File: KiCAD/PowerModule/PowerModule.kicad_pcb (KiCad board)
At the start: 2 copper layers, 90 x 70 mm, 41 parts, among them J1 GPU, J2 BATTERY, J3 BUS, J4 MONITOR, J5 MASTER, J6 Conn_01x02, J7 Conn_01x02, Q3 AO3401A, Q5 AO3401A, U2 INA219BxDCN, U3 INA219BxDCN, U4 INA219BxDCN

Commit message: 塗りつぶしとクリアランスの設定を変更．エラーは無し．
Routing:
- net +3.3V: track 67.1 -> 70.2 mm, vias 1 -> 3
- net GND: vias 59 -> 58
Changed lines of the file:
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@@
 	)
 	(setup
+		(stackup
+			(layer "F.SilkS"
+				(type "Top Silk Screen")
+			)
+			(layer "F.Paste"
+				(type "Top Solder Paste")
+			)
+			(layer "F.Mask"
+				(type "Top Solder Mask")
+				(thickness 0.01)
+			)
+			(layer "F.Cu"
+				(type "copper")
+				(thickness 0.035)
+			)
+			(layer "dielectric 1"
+				(type "core")
+				(thickness 1.51)
+				(material "FR4")
+				(epsilon_r 4.5)
+				(loss_tangent 0.02)
+			)
+			(layer "B.Cu"
+				(type "copper")
+				(thickness 0.035)
+			)
+			(layer "B.Mask"
+				(type "Bottom Solder Mask")
+				(thickness 0.01)
+			)
+			(layer "B.Paste"
+				(type "Bottom Solder Paste")
+			)
+			(layer "B.SilkS"
+				(type "Bottom Silk Screen")
+			)
+			(copper_finish "None")
+			(dielectric_constraints no)
+		)
 		(pad_to_mask_clearance 0)
 		(allow_soldermask_bridges_in_footprints no)
@@
 	)
 	(via
-		(at 176.19764 134.36)
-		(size 0.6)
-		(drill 0.3)
-		(layers "F.Cu" "B.Cu")
-		(free yes)
-		(net 2)
-	)
-	(via
 		(at 144 134)
 		(size 0.6)
@@
 	)
 	(segment
-		(start 122.4 96.05)
-		(end 123.35 96.05)
-		(width 0.25)
+		(start 124.675 93.257)
+		(end 124.675 94.1)
+		(width 0.2)
 		(layer "F.Cu")
 		(net 8)
 	)
 	(segment
-		(start 124.675 94.174)
-		(end 124.675 94.1)
-		(width 0.25)
+		(start 122.428 96.078)
+		(end 122.4 96.05)
+		(width 0.2)
 		(layer "F.Cu")
 		(net 8)
@@
 	)
 	(segment
+		(start 122.428 96.774)
+		(end 122.428 96.078)
+		(width 0.2)
+		(layer "F.Cu")
+		(net 8)
+	)
+	(segment
 		(start 124.037501 99.55)
 		(end 124.7 99.55)
@@
 	)
 	(segment
-		(start 123.35 96.05)
-		(end 123.5 95.9)
-		(width 0.25)
-		(layer "F.Cu")
-		(net 8)
-	)
-	(segment
 		(start 130.8375 94.1)
 		(end 130.8375 99.6)
@@
 	)
 	(segment
-		(start 123.5 95.9)
-		(end 123.5 94.5)
-		(width 0.25)
-		(layer "F.Cu")
-		(net 8)
-	)
-	(segment
 		(start 130.8375 99.6)
 		(end 130.8375 106.2)
@@
 	)
 	(segment
+		(start 124.714 93.218)
+		(end 124.675 93.257)
+		(width 0.2)
+		(layer "F.Cu")
+		(net 8)
+	)
+	(segment
 		(start 146.9875 124.4875)
 		(end 146.9875 122.4)
@@
 	)
 	(segment
-		(start 123.5 94.5)
-		(end 123.826 94.174)
-		(width 0.25)
-		(layer "F.Cu")
-		(net 8)
-	)
-	(segment
 		(start 130.8375 99.6)
 		(end 130.0375 98.8)
@@
 		(net 8)
 	)
-	(segment
-		(start 123.826 94.174)
-		(end 124.675 94.174)
-		(width 0.25)
-		(layer "F.Cu")
+	(via
+		(at 130.9 110.9)
+		(size 0.6)
+		(drill 0.3)
+		(layers "F.Cu" "B.Cu")
 		(net 8)
 	)
 	(via
-		(at 130.9 110.9)
+		(at 122.428 96.774)
 		(size 0.6)
 		(drill 0.3)
@@
 		(net 8)
 	)
+	(via
+		(at 124.714 93.218)
+		(size 0.6)
+		(drill 0.3)
+		(layers "F.Cu" "B.Cu")
+		(net 8)
+	)
+	(segment
+		(start 122.428 96.774)
+		(end 123.19 96.774)
+		(width 0.2)
+		(layer "B.Cu")
+		(net 8)
+	)
 	(segment
 		(start 132.7 111.6)
@@
 	)
 	(segment
+		(start 123.952 93.218)
+		(end 124.714 93.218)
+		(width 0.2)
+		(layer "B.Cu")
+		(net 8)
+	)
+	(segment
 		(start 131.6 111.6)
 		(end 132.7 111.6)
@@
 	)
 	(segment
+		(start 123.444 93.726)
+		(end 123.952 93.218)
+		(width 0.2)
+		(layer "B.Cu")
+		(net 8)
+	)
+	(segment
+		(start 123.19 96.774)
+		(end 123.444 96.52)
+		(width 0.2)
+		(layer "B.Cu")
+		(net 8)
+	)
+	(segment
 		(start 130.9 110.9)
 		(end 131.6 111.6)
@@
 	)
 	(segment
+		(start 123.444 96.52)
+		(end 123.444 93.726)
+		(width 0.2)
+		(layer "B.Cu")
+		(net 8)
+	)
+	(segment
 		(start 145.65 124.55)
 		(end 147 124.55)
@@
 		(layers "F.Cu" "B.Cu")
 		(hatch edge 0.5)
-		(connect_pads
+		(connect_pads yes
 			(clearance 0.25)
 		)

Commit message: Power Build-1,Battery Build-1完成
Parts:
- added G***: LOGO, LOGO, B.Cu at (162.9, 131.2)
- added G***: LOGO, LOGO, B.Cu at (136.9, 131.8)
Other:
- outline, holes or cut-outs redrawn
- board text added: "CAPACITOR"
- board text added: "Power Module Build-1"
- board text added: "SUBARU"
- board text added: "Tokai Student Rocket Project"
- board text added: "U1"
- board text added: "V1.3"
- board text removed: "capacitor"

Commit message: 取り付け穴位置を更新
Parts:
- J7: value Conn_01x02 -> DF1B-2S-2.5R
- moved H1 5.83 mm to (120.0, 128.0)
- moved H2 5.83 mm to (120.0, 72.0)
- moved H3 5.83 mm to (180.0, 128.0)
- moved H4 5.83 mm to (180.0, 72.0)
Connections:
- H1 pad 1: GND -> (no net)
- H2 pad 1: GND -> (no net)
- H3 pad 1: GND -> (no net)
- H4 pad 1: GND -> (no net)
- J7 pad 1: Net-(D3-A) -> GND
- J7 pad 2: unconnected-(J7-Pin_2-Pad2) -> Net-(D3-A)
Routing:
- net VREF_T1: track 26.9 -> 15.8 mm
- net Net-(D3-A): track 19.5 -> 22.4 mm
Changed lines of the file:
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@@
 	(net 33 "Net-(U1-PGD)")
 	(net 34 "+5V")
-	(net 35 "unconnected-(J7-Pin_2-Pad2)")
 	(footprint "Resistor_SMD:R_0603_1608Metric"
 		(layer "F.Cu")
@@
 	(footprint "MountingHole:MountingHole_3.2mm_M3_DIN965_Pad_TopBottom"
 		(layer "F.Cu")
-		(at 125 125)
+		(at 120 128)
 		(descr "Mounting Hole 3.2mm, M3, DIN965")
 		(tags "mounting hole 3.2mm m3 din965")
@@
 			(layers "*.Cu" "*.Mask")
 			(remove_unused_layers no)
-			(net 2 "GND")
 		)
 		(pad "1" connect circle
@@
 			(size 5.6 5.6)
 			(layers "F.Cu" "F.Mask")
-			(net 2 "GND")
 		)
 		(pad "1" connect circle
@@
 			(size 5.6 5.6)
 			(layers "B.Cu" "B.Mask")
-			(net 2 "GND")
 		)
 		(embedded_fonts no)
@@
 	(footprint "MountingHole:MountingHole_3.2mm_M3_DIN965_Pad_TopBottom"
 		(layer "F.Cu")
-		(at 175 75)
+		(at 180 72)
 		(descr "Mounting Hole 3.2mm, M3, DIN965")
 		(tags "mounting hole 3.2mm m3 din965")
@@
 			(layers "*.Cu" "*.Mask")
 			(remove_unused_layers no)
-			(net 2 "GND")
 		)
 		(pad "1" connect circle
@@
 			(size 5.6 5.6)
 			(layers "F.Cu" "F.Mask")
-			(net 2 "GND")
 		)
 		(pad "1" connect circle
@@
 			(size 5.6 5.6)
 			(layers "B.Cu" "B.Mask")
-			(net 2 "GND")
 		)
 		(embedded_fonts no)
@@
 	(footprint "MountingHole:MountingHole_3.2mm_M3_DIN965_Pad_TopBottom"
 		(layer "F.Cu")
-		(at 175 125)
+		(at 180 128)
 		(descr "Mounting Hole 3.2mm, M3, DIN965")
 		(tags "mounting hole 3.2mm m3 din965")
@@
 			(layers "*.Cu" "*.Mask")
 			(remove_unused_layers no)
-			(net 2 "GND")
 		)
 		(pad "1" connect circle
@@
 			(size 5.6 5.6)
 			(layers "F.Cu" "F.Mask")
-			(net 2 "GND")
 		)
 		(pad "1" connect circle
@@
 			(size 5.6 5.6)
 			(layers "B.Cu" "B.Mask")
-			(net 2 "GND")
 		)
 		(embedded_fonts no)
@@
 			)
 		)
-		(property "Value" "Conn_01x02"
+		(property "Value" "DF1B-2S-2.5R"
 			(at 0 -8.1 180)
 			(unlocked yes)
@@
 			(layers "*.Cu" "*.Mask")
 			(remove_unused_layers no)
-			(net 9 "Net-(D3-A)")
+			(net 2 "GND")
 			(pinfunction "Pin_1")
 			(pintype "passive")
@@
 			(layers "*.Cu" "*.Mask")
 			(remove_unused_layers no)
-			(net 35 "unconnected-(J7-Pin_2-Pad2)")
+			(net 9 "Net-(D3-A)")
 			(pinfunction "Pin_2")
-			(pintype "passive+no_connect")
+			(pintype "passive")
 			(solder_mask_margin 0.1016)
 			(thermal_bridge_angle 45)
@@
 	(footprint "MountingHole:MountingHole_3.2mm_M3_DIN965_Pad_TopBottom"
 		(layer "F.Cu")
-		(at 125 75)
+		(at 120 72)
 		(descr "Mounting Hole 3.2mm, M3, DIN965")
 		(tags "mounting hole 3.2mm m3 din965")
@@
 			(layers "*.Cu" "*.Mask")
 			(remove_unused_layers no)
-			(net 2 "GND")
 		)
 		(pad "1" connect circle
@@
 			(size 5.6 5.6)
 			(layers "F.Cu" "F.Mask")
-			(net 2 "GND")
 		)
 		(pad "1" connect circle
@@
 			(size 5.6 5.6)
 			(layers "B.Cu" "B.Mask")
-			(net 2 "GND")
 		)
 		(embedded_fonts no)
@@
 	)
 	(gr_text "BAT SW"
-		(at 151.8 66.6 180)
+		(at 151.962 54.483 180)
 		(layer "F.SilkS" knockout)
 		(effects
@@
 	)
 	(gr_text "BATTERY\n"
-		(at 133.9 66.6 180)
+		(at 127.254 55.118 180)
 		(layer "F.SilkS" knockout)
 		(effects
@@
 	)
 	(gr_text "SW"
-		(at 160.038 66.5 180)
+		(at 161.036 54.61 180)
 		(layer "F.SilkS" knockout)
 		(effects
@@
 	)
 	(gr_text "CAPACITOR\n"
-		(at 142.9 66.8 180)
+		(at 142.962 58.674 180)
 		(layer "F.SilkS" knockout)
 		(effects
@@
 	)
 	(segment
-		(start 144.232 75.712)
-		(end 144.232 79.032)
+		(start 152.0875 84.2125)
+		(end 153.3 83)
 		(width 0.5)
 		(layer "F.Cu")
@@
 	)
 	(segment
-		(start 153.3 83)
-		(end 148.2 83)
+		(start 141.732 79.629)
+		(end 141.732 75.752)
 		(width 0.5)
 		(layer "F.Cu")
@@
 	)
 	(segment
-		(start 152.0875 84.2125)
-		(end 153.3 83)
+		(start 145.103 83)
+		(end 141.732 79.629)
 		(width 0.5)
 		(layer "F.Cu")
@@
 	)
 	(segment
-		(start 148.2 83)
-		(end 144.232 79.032)
+		(start 153.3 83)
+		(end 145.103 83)
+		(width 0.5)
+		(layer "F.Cu")
+		(net 9)
+	)
+	(segment
+		(start 141.732 75.752)
+		(end 141.692 75.712)
 		(width 0.5)
 		(layer "F.Cu")
@@
 	)
 	(segment
-		(start 154.6 129.2)
-		(end 154.6 123.2)
-		(width 0.2)
-		(layer "B.Cu")
-		(net 22)
-	)
-	(segment
-		(start 154.6 123.2)
-		(end 154.1 122.7)
+		(start 149.987 125.563)
+		(end 151 124.55)
 		(width 0.2)
 		(layer "B.Cu")
@@
 	)
 	(segment
-		(start 154.1 122.7)
-		(end 152.85 122.7)
+		(start 145.410668 132)
+		(end 149.987 127.423668)
 		(width 0.2)
 		(layer "B.Cu")
@@
 	)
 	(segment
-		(start 151.8 132)
-		(end 154.6 129.2)
+		(start 143.5 132)
+		(end 145.410668 132)
 		(width 0.2)
 		(layer "B.Cu")
@@
 	)
 	(segment
-		(start 152.85 122.7)
-		(end 151 124.55)
+		(start 149.987 127.423668)
+		(end 149.987 125.563)
 		(width 0.2)
 		(layer "B.Cu")
@@
 	)
 	(segment
-		(start 143.5 132)
-		(end 151.8 132)
-		(width 0.2)
-		(layer "B.Cu")
-		(net 22)
-	)
-	(segment
 		(start 158.73 77.73)
 		(end 158.73 75.712)
@@
 	)
 	(segment
-		(start 148.7839 126.149)
-		(end 149 126.149)
-		(width 0.2)
-		(layer "F.Cu")
-		(net 28)
-	)
-	(segment
 		(start 119.975 106.125)
 		(end 119.2 106.9)
@@
 		(layers "F.Cu" "B.Cu")
 		(hatch edge 0.5)
-		(connect_pads yes
+		(connect_pads
 			(clearance 0.25)
 		)
@@
 		(polygon
 			(pts
-				(xy 86.1 68) (xy 89.005402 145.4557) (xy 191.4 140.3) (xy 207 60.6) (xy 101.1 59.6)
+				(xy 122 60) (xy 100 80) (xy 100 120) (xy 120 140) (xy 180 140) (xy 200 120) (xy 200 80) (xy 180 60)
 			)
 		)

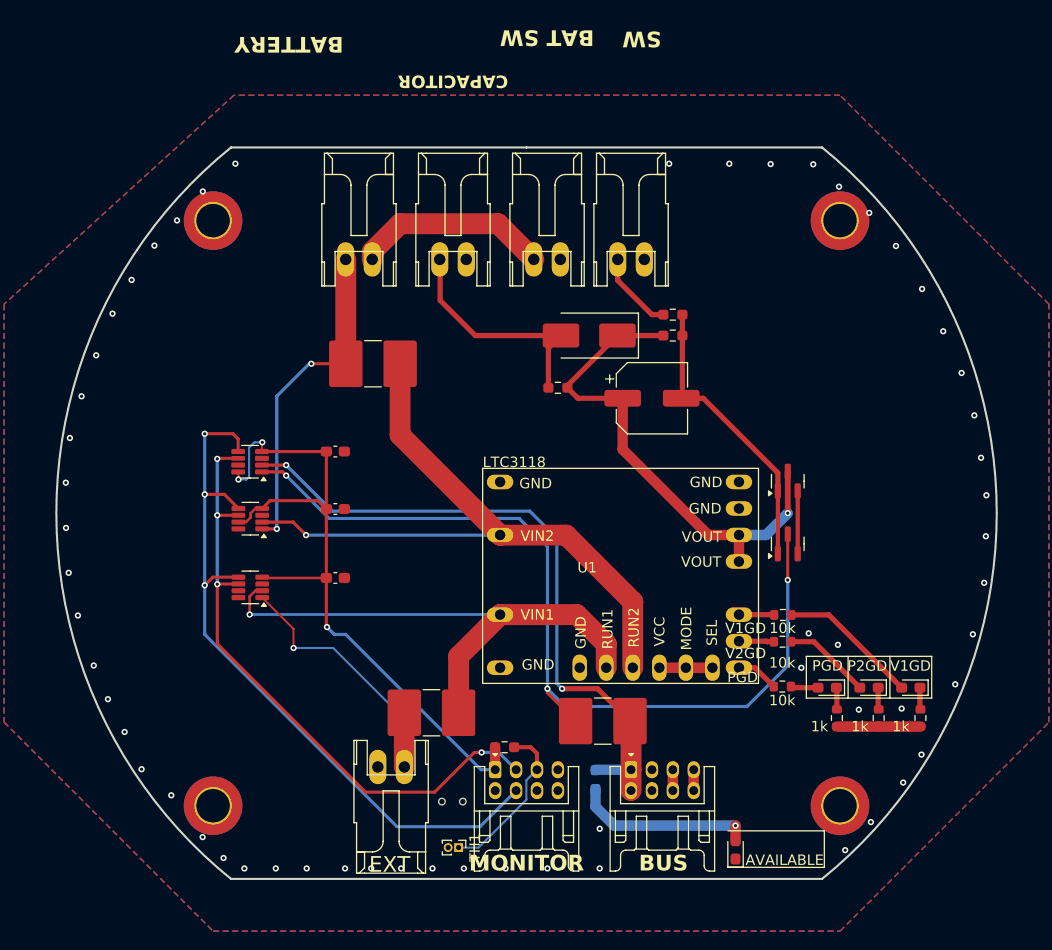
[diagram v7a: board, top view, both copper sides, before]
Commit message: 3Dモデルを組み合わせて結合試験する
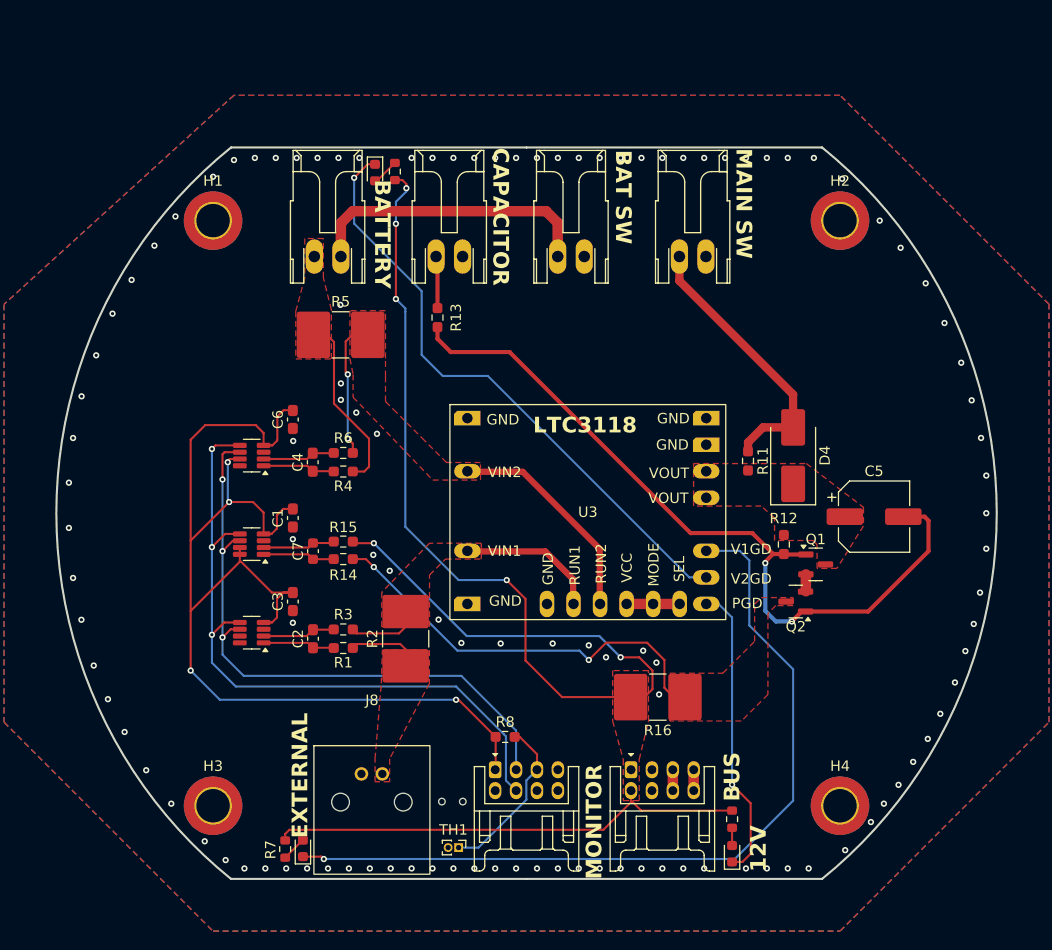
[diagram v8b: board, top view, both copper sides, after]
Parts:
- removed C16: 33uF, Capacitor_SMD:CP_Elec_6.3x5.9
- removed D5, D6: Orange, LED_SMD:LED_0603_1608Metric_Pad1.05x0.95mm_HandSolder
- removed D7: Green, LED_SMD:LED_0603_1608Metric_Pad1.05x0.95mm_HandSolder
- removed J1: GPU, TSRP_Connector_Hirose:DF1B-2S-2.5R
- removed Q3, Q5: AO3401A, Package_TO_SOT_SMD:SOT-23
- removed R17: 5.6kR, Resistor_SMD:R_0603_1608Metric_Pad0.98x0.95mm_HandSolder
- removed R18: 3.3kR, Resistor_SMD:R_0603_1608Metric_Pad0.98x0.95mm_HandSolder
- removed R19: 0.1R, Resistor_SMD:R_2816_7142Metric_Pad3.20x4.45mm_HandSolder
- added C1: 0.1uF, Capacitor_SMD:C_0603_1608Metric_Pad1.08x0.95mm_HandSolder, F.Cu at (127.6, 100.5)
- added C2: 0.1uF, Capacitor_SMD:C_0603_1608Metric_Pad1.08x0.95mm_HandSolder, F.Cu at (129.6, 112.0)
- added C3: 0.1uF, Capacitor_SMD:C_0603_1608Metric_Pad1.08x0.95mm_HandSolder, F.Cu at (127.6, 108.5)
- added C7: 0.1uF, Capacitor_SMD:C_0603_1608Metric, F.Cu at (129.6, 103.6)
- added D1: Orange, LED_SMD:LED_0603_1608Metric, F.Cu at (128.6, 132.1)
- added D2: Orange, LED_SMD:LED_0603_1608Metric, F.Cu at (135.5, 67.4)
- added J8: DF51-2P-2DS, TSRP_Connector_Hirose:DF51-2P-2DS, F.Cu at (135.2, 134.4)
- added Q1: AO3401A, Package_TO_SOT_SMD:SOT-23, F.Cu at (177.7, 104.9)
- added Q2: AO3401A, Package_TO_SOT_SMD:SOT-23, F.Cu at (175.8, 108.5)
- added R12: 5.6kR, Resistor_SMD:R_0603_1608Metric_Pad0.98x0.95mm_HandSolder, F.Cu at (174.6, 103.0)
- added R14: 10R, Resistor_SMD:R_0603_1608Metric_Pad0.98x0.95mm_HandSolder, F.Cu at (132.5, 104.4)
- added R15: 10R, Resistor_SMD:R_0603_1608Metric_Pad0.98x0.95mm_HandSolder, F.Cu at (132.5, 102.7)
- added R16: 0.1R, Resistor_SMD:R_2816_7142Metric_Pad3.20x4.45mm_HandSolder, F.Cu at (162.6, 117.6)
- added R4: 10R, Resistor_SMD:R_0603_1608Metric_Pad0.98x0.95mm_HandSolder, F.Cu at (132.5, 96.0)
- C5: value 0.1uF -> 33uF; footprint Capacitor_SMD:C_0603_1608Metric_Pad1.08x0.95mm_HandSolder -> Capacitor_SMD:CP_Elec_6.3x5.9
- D3: value SR54F -> Orange; footprint Diode_SMD:D_SMB_Handsoldering -> LED_SMD:LED_0603_1608Metric
- D4: value Orange -> SR54F; footprint LED_SMD:LED_0603_1608Metric_Pad1.05x0.95mm_HandSolder -> Diode_SMD:D_SMB_Handsoldering
- H1, H2, H3, H4: value MountingHole -> MountingHole_Pad
- J2: renamed from J6; value Conn_01x02 -> DF1B-2S-2.5R
- J3: renamed from J2; value BATTERY -> DF1B-2S-2.5R
- J5: renamed from J3; value BUS -> DF11-8DP-2DS
- J6: renamed from J5; value MASTER -> DF1B-2S-2.5R
- J7: renamed from J4; value MONITOR -> DF11-8DP-2DS
- R1: value 10k -> 10R; footprint Resistor_SMD:R_0603_1608Metric -> Resistor_SMD:R_0603_1608Metric_Pad0.98x0.95mm_HandSolder
- R10: value 10k -> 2.4kR
- R11: value 1k -> 5.6kR; footprint Resistor_SMD:R_0603_1608Metric -> Resistor_SMD:R_0603_1608Metric_Pad0.98x0.95mm_HandSolder
- R13: value 10kR -> 3.3kR
- R2: value 10k -> 0.1R; footprint Resistor_SMD:R_0603_1608Metric -> Resistor_SMD:R_2816_7142Metric_Pad3.20x4.45mm_HandSolder
- R3: value 0.1R -> 10R; footprint Resistor_SMD:R_2816_7142Metric_Pad3.20x4.45mm_HandSolder -> Resistor_SMD:R_0603_1608Metric_Pad0.98x0.95mm_HandSolder
- R6: value 5.6kR -> 10R
- R7: value 2.7kR -> 2.4kR; footprint Resistor_SMD:R_0603_1608Metric_Pad0.98x0.95mm_HandSolder -> Resistor_SMD:R_0603_1608Metric; moved to F.Cu
- R8: value 1k -> 10kR; footprint Resistor_SMD:R_0603_1608Metric -> Resistor_SMD:R_0603_1608Metric_Pad0.98x0.95mm_HandSolder
- R9: value 1k -> 2.4kR
- moved R9 67.3 mm to (137.4, 67.3)
- moved H2 60.0 mm to (180.0, 72.0)
- moved H3 60.0 mm to (120.0, 128.0)
- moved H1 56.0 mm to (120.0, 72.0)
- moved H4 56.0 mm to (180.0, 128.0)
- moved C5 51.9 mm to (183.3, 100.3), turned to 0 degrees
- moved D3 51.4 mm to (169.7, 132.6), turned to 90 degrees
- moved R5 44.7 mm to (132.2, 82.9)
- moved R1 42.0 mm to (132.5, 112.9)
- moved R13 41.6 mm to (141.5, 81.3), turned to 90 degrees
- moved R2 36.3 mm to (138.4, 112.0), turned to 90 degrees
- moved R8 35.8 mm to (148.0, 121.4), turned to 0 degrees
- moved R7 30.4 mm to (126.9, 132.1)
- moved R11 29.6 mm to (171.2, 95.0)
- moved J4 22.9 mm to (165.9, 74.7)
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- renumbered J7 to J4, U3 to U1, U1 to U3
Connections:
- C4 pad 1: GND -> Net-(U2-IN+)
- C4 pad 2: +3.3V -> Net-(U2-IN-)
- C5 pad 1: GND -> /VOUT
- C5 pad 2: +3.3V -> Net-(Q1-G)
- D4 pad 1: Net-(D4-K) -> /VOUT
- H1 pad 1: (no net) -> GND
- H2 pad 1: (no net) -> GND
- H3 pad 1: (no net) -> GND
- H4 pad 1: (no net) -> GND
- J3 pad 2: Net-(J2-Pin_2) (its old number) -> /BAT IN
- J4 pad 2: Net-(D3-A) -> Net-(D4-A)
- J6 pad 2: Net-(J5-Pin_2) -> Net-(J6-Pin_2)
- R1 pad 1: Net-(U1-V2GD) -> Net-(U1-IN+)
- R1 pad 2: Net-(D5-A) -> /GPU IN
- R10 pad 1: Net-(U1-V1GD) -> Net-(D3-A)
- R10 pad 2: Net-(D6-A) -> +12V
- R11 pad 1: Net-(D6-K) -> Net-(D4-A)
- R11 pad 2: +5V -> /VOUT
- R13 pad 1: +3.3V -> Net-(Q1-G)
- R13 pad 2: VREF_T1 -> Net-(J6-Pin_2)
- R2 pad 1: Net-(U1-PGD) -> /GPU IN
- R2 pad 2: Net-(D4-A) -> /GPU OUT
- R3 pad 1: Net-(J1-Pin_2) -> Net-(U1-IN-)
- R3 pad 2: Net-(U1-RUN1) -> /GPU OUT
- R5 pad 1: Net-(Q5-S) -> /BAT IN
- R5 pad 2: +12V -> /BAT OUT
- R6 pad 1: Net-(D3-A) -> Net-(U2-IN-)
- R6 pad 2: Net-(D3-K) -> /BAT OUT
- R8 pad 1: Net-(D5-K) -> +3.3V
- R8 pad 2: +5V -> VREF_T1
- R9 pad 1: Net-(D4-K) -> Net-(D2-A)
- R9 pad 2: +5V -> +12V
- U1 pad 1: Net-(J1-Pin_2) -> Net-(U1-IN+)
- U1 pad 2: Net-(U1-RUN1) -> Net-(U1-IN-)
- U2 pad 1: Net-(J2-Pin_2) (its old number) -> Net-(U2-IN+)
- U2 pad 2: Net-(U1-RUN2) -> Net-(U2-IN-)
- U3 pad 11: Net-(U1-PGD) -> Net-(D3-K)
- U3 pad 12: Net-(U1-V2GD) -> Net-(D2-K)
- U3 pad 13: Net-(U1-V1GD) -> Net-(D1-K)
- U3 pad 14: Net-(D3-K) -> /VOUT
- U3 pad 15: Net-(D3-K) -> /VOUT
- U3 pad 2: Net-(U1-RUN2) -> /BAT OUT
- U3 pad 3: Net-(U1-RUN1) -> /GPU OUT
- U3 pad 6: Net-(U1-RUN1) -> /GPU OUT
- U3 pad 7: Net-(U1-RUN2) -> /BAT OUT
- U4 pad 1: Net-(Q5-S) -> Net-(U4-IN+)
- U4 pad 2: +12V -> Net-(U4-IN-)
- U4 pad 7: GND -> +3.3V
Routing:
- net +12V: track 64.9 -> 151.6 mm, vias 2 -> 6
- net Net-(Q5-S): track 86.0 -> 0.00 mm, vias 3 -> 0
- net Net-(D1-K): track 0.00 -> 78.6 mm, vias 0 -> 1
- net Net-(Q1-G): track 0.00 -> 76.0 mm, vias 0 -> 2
- net Net-(U1-RUN2): track 65.6 -> 0.00 mm, vias 1 -> 0
- net Net-(D2-K): track 0.00 -> 58.2 mm, vias 0 -> 1
- net Net-(U1-RUN1): track 52.4 -> 0.00 mm, vias 1 -> 0
- net +3.3V: track 70.2 -> 111.9 mm, vias 3 -> 4
- net /BUS IN: track 0.00 -> 40.2 mm, vias 0 -> 2
- net /BAT OUT: track 0.00 -> 34.4 mm, vias 0 -> 2
- net Net-(J2-Pin_2) (its old number): track 32.0 -> 0.00 mm, vias 2 -> 0
- net Net-(J1-Pin_2): track 29.3 -> 0.00 mm, vias 1 -> 0
- net Net-(Q3-G): track 28.0 -> 0.00 mm
- net Net-(D4-A): track 2.64 -> 26.6 mm
- net /GPU OUT: track 0.00 -> 20.9 mm
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- added copper zone on F.Cu, net +12V
- added copper zone on F.Cu, net /BAT IN
- added copper zone on F.Cu, net /BAT OUT
- added copper zone on F.Cu, net /BUS IN
- added copper zone on F.Cu, net /GPU IN
- added copper zone on F.Cu, net /GPU OUT
- added copper zone on F.Cu, net /VOUT
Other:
- board text added: "12V"
- board text added: "EXTERNAL"
- board text added: "MAIN SW"
- board text removed: "10k"
- board text removed: "1k"
- board text removed: "AVAILABLE"
- board text removed: "EXT"
- board text removed: "P2GD"
- board text removed: "PGD"
- board text removed: "SW"
- board text removed: "U1"
- board text removed: "V1GD"
